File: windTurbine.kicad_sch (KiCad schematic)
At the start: 12 parts, among them M1 Motor_Servo, M2 LP-MSPM0G3507

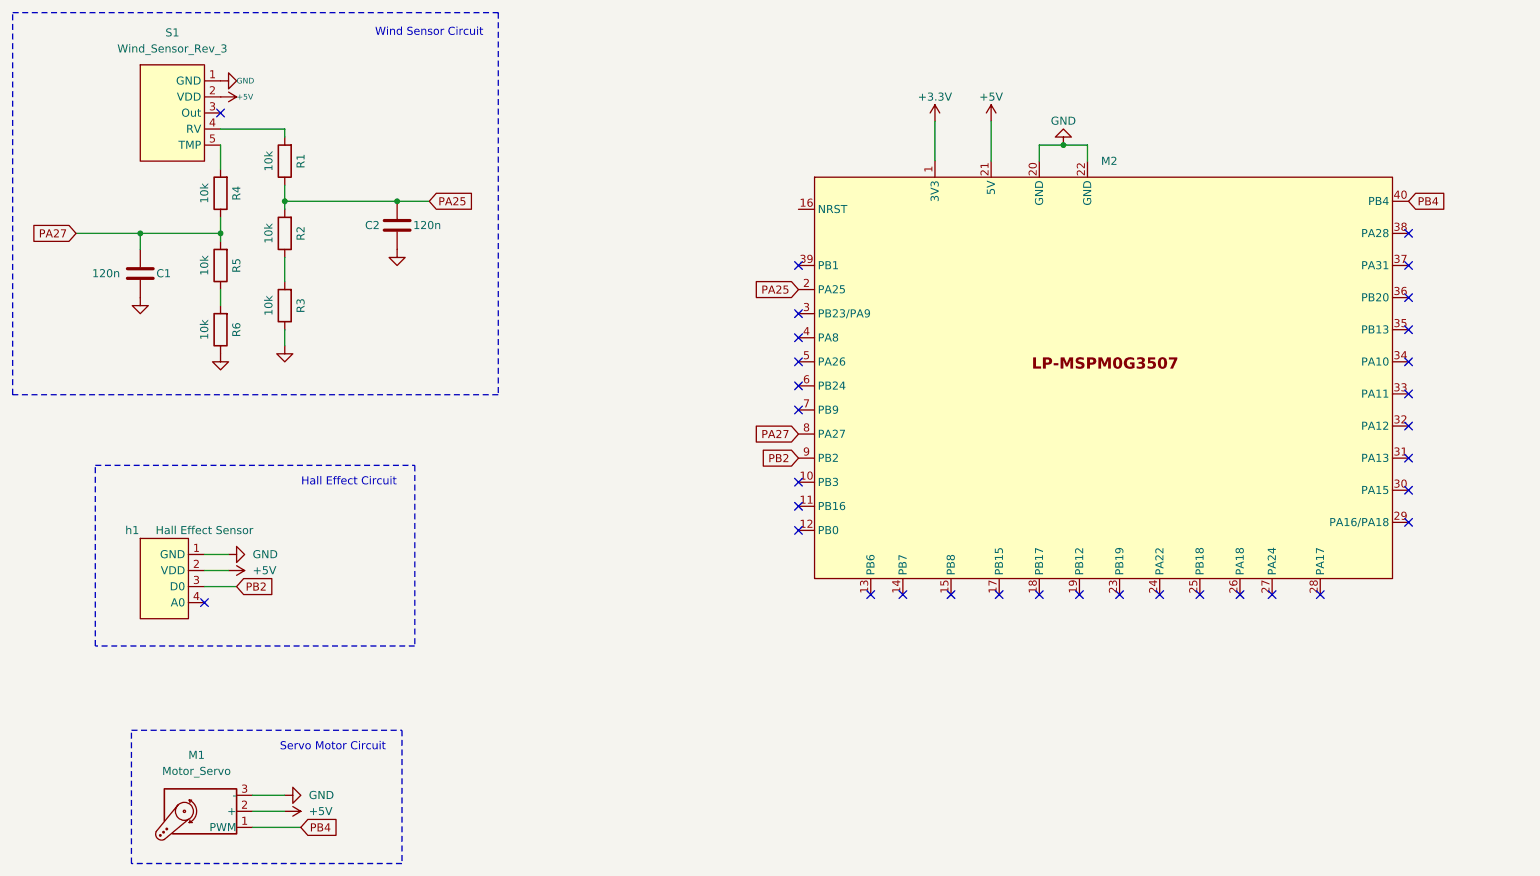
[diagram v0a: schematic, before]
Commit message: Schematic Change. Rearranged Components
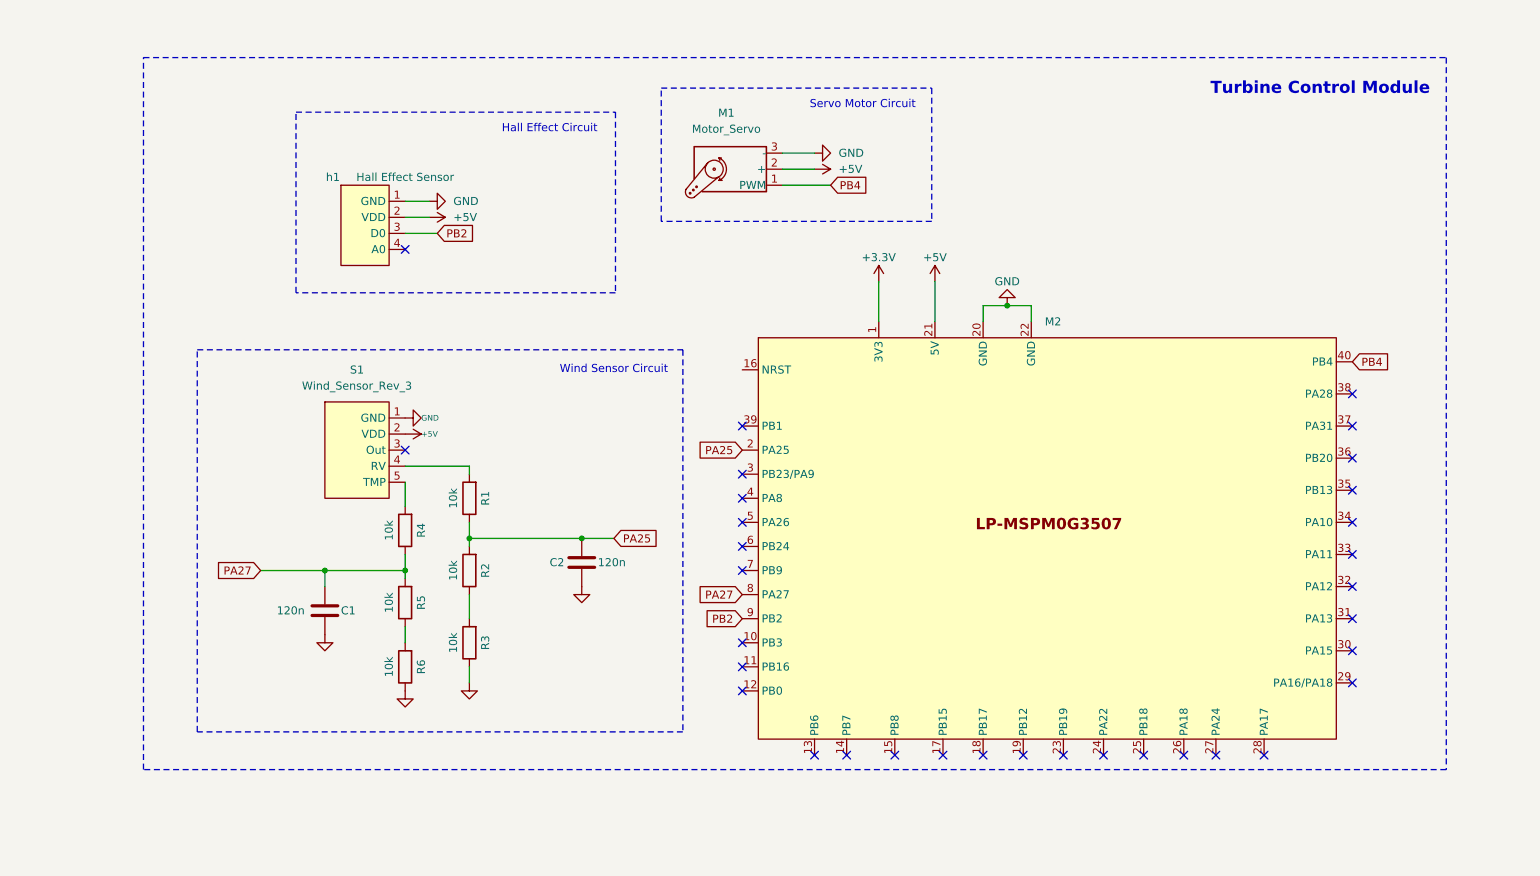
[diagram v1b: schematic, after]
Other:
- note added: "Turbine Control Module"
- moved on the sheet: C1, C2, M1, M2, R1, R2, R3, R4, R5, R6, S1, h1

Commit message: Load MCU
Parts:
- removed C1, C2: 120n, symbol Device:C
- removed M1: Motor_Servo, symbol Motor:Motor_Servo
- removed M2: LP-MSPM0G3507, symbol Turbine_MCU:LP-MSPM0G3507
- removed R1, R2, R3, R4, R5, R6: 10k, symbol Device:R
- removed S1: Wind_Sensor_Rev_3, symbol windTurbineSchemSymLib:Wind_Sensor_Rev_C
- removed h1: Hall Effect Sensor, symbol windTurbineSchemSymLib:hall_effect_sensor
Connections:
- no-connect marks 33 -> 0
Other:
- added sheet Load & MCU Module (load_and_mcu_module.kicad_sch)
- added sheet Turbine Module (turbine_module.kicad_sch)
- note removed: "Hall Effect Circuit"
- note removed: "Servo Motor Circuit"
- note removed: "Turbine Control Module"
- note removed: "Wind Sensor Circuit"

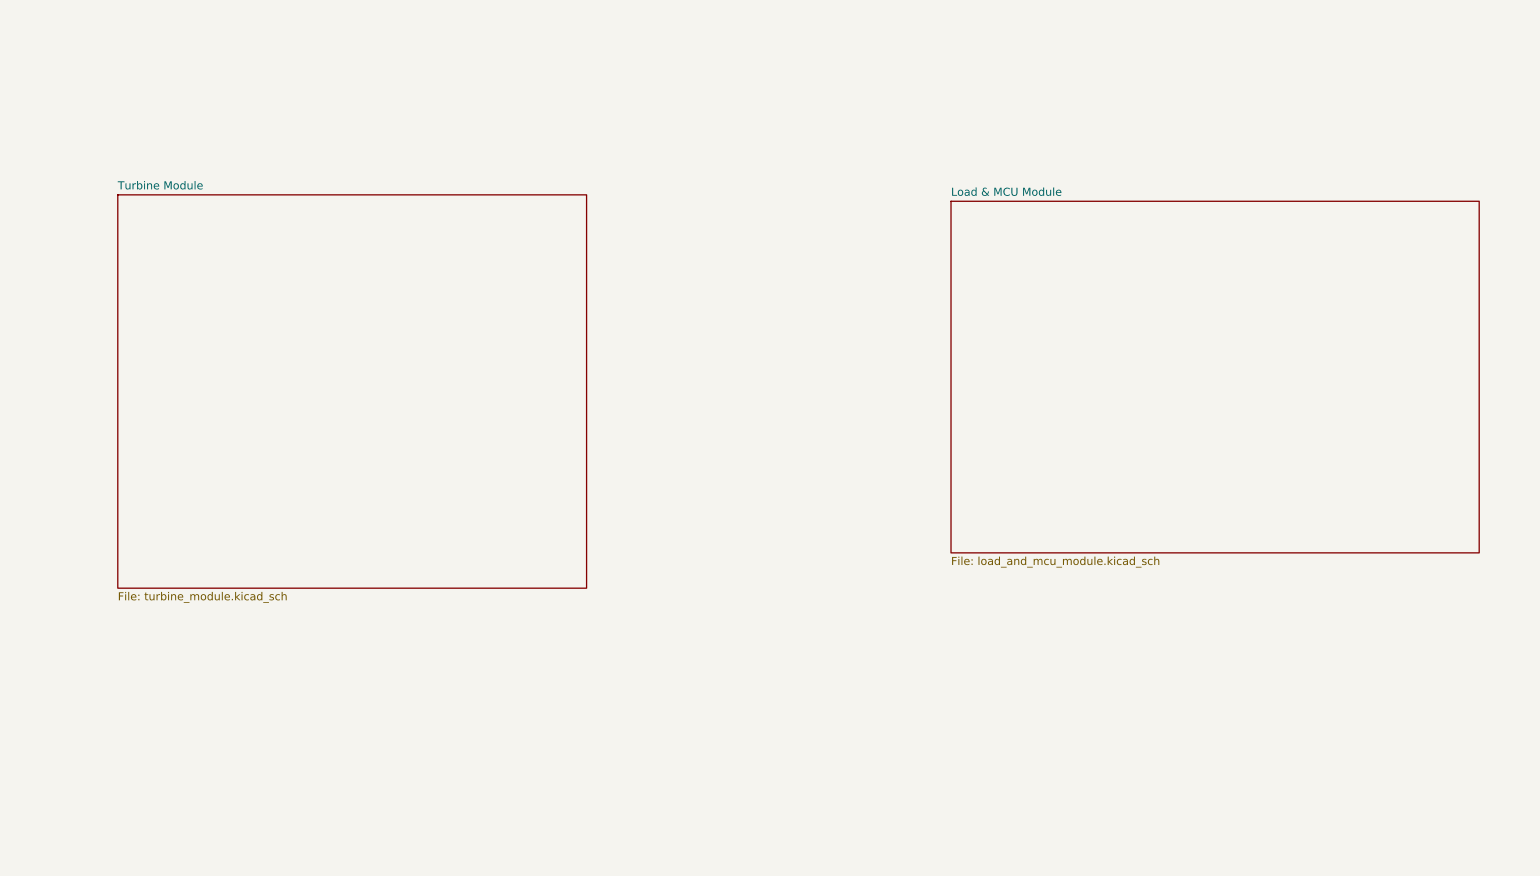
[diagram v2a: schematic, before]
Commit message: Finished Squematics V1
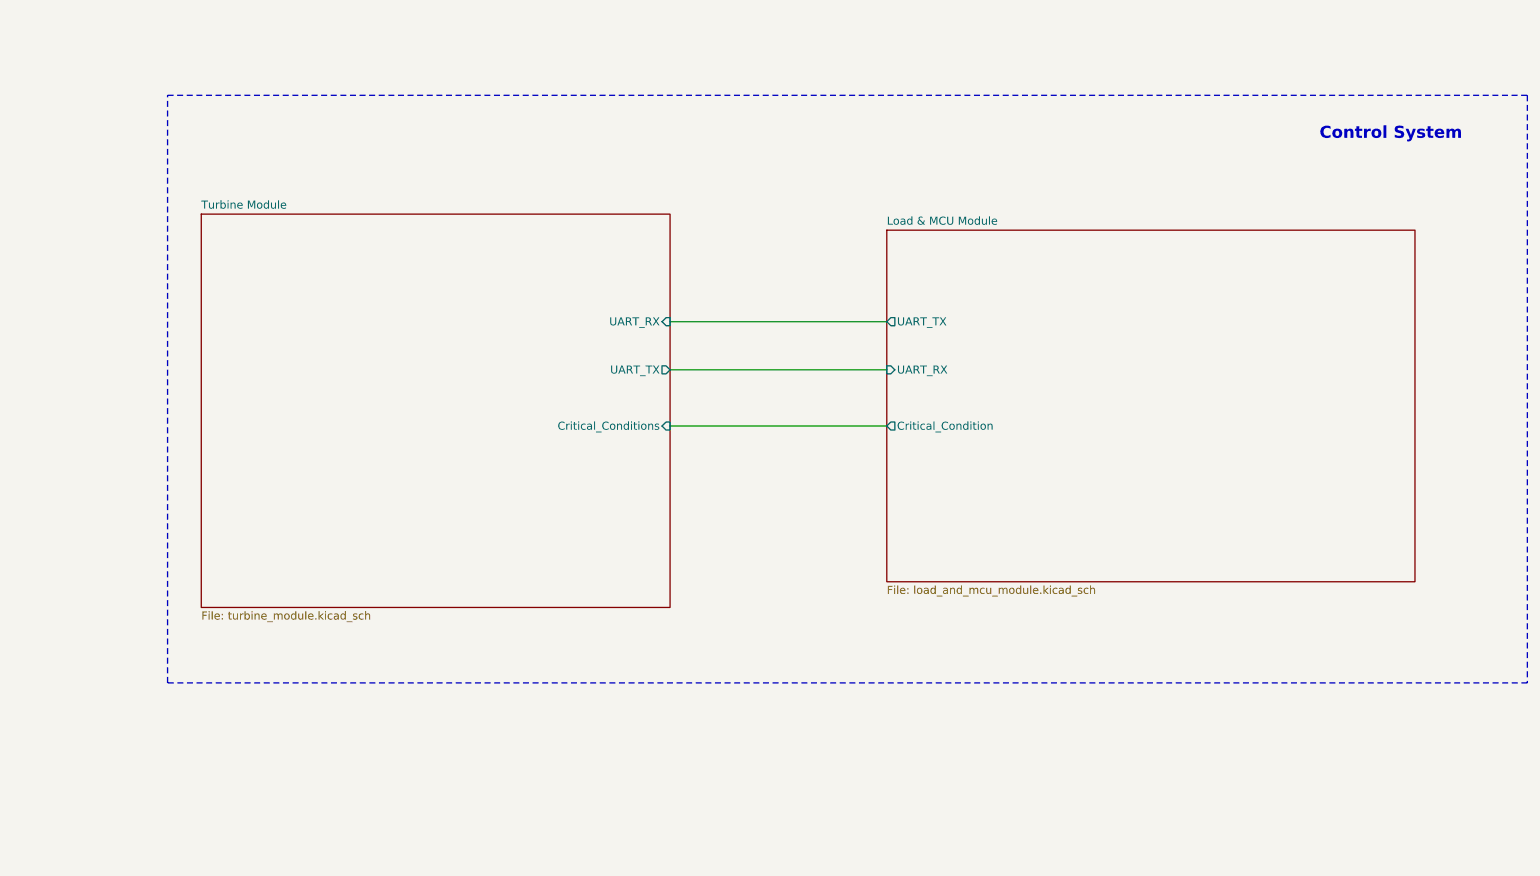
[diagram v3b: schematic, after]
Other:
- sheet Load & MCU Module ports: added Critical_Condition, UART_RX, UART_TX; removed none
- sheet Turbine Module ports: added Critical_Conditions, UART_RX, UART_TX; removed none
- note added: "Control System"
- title: Pitch Control Submodule -> Control System
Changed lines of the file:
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@@
 	(paper "A4")
 	(title_block
-		(title "Pitch Control Submodule")
+		(title "Control System")
 		(date "2026-03-15")
 		(rev "A")
 		(company "Puerto Rico Embedded Solutions")
 	)
+	(rectangle
+		(start 44.958 41.656)
+		(end 260.096 134.62)
+		(stroke
+			(width 0)
+			(type dash)
+		)
+		(fill
+			(type none)
+		)
+	)
+	(text "Control System "
+		(exclude_from_sim no)
+		(at 238.506 47.752 0)
+		(effects
+			(font
+				(size 1.905 1.905)
+				(thickness 0.254)
+				(bold yes)
+			)
+		)
+	)
+	(wire
+		(pts
+			(xy 124.46 85.09) (xy 158.75 85.09)
+		)
+		(stroke
+			(width 0)
+			(type default)
+		)
+	)
+	(wire
+		(pts
+			(xy 124.46 93.98) (xy 158.75 93.98)
+		)
+		(stroke
+			(width 0)
+			(type default)
+		)
+	)
+	(wire
+		(pts
+			(xy 124.46 77.47) (xy 158.75 77.47)
+		)
+		(stroke
+			(width 0)
+			(type default)
+		)
+	)
 	(sheet
-		(at 37.084 57.404)
+		(at 50.292 60.452)
 		(size 74.168 62.23)
 		(exclude_from_sim no)
@@
 		)
 		(property "Sheetname" "Turbine Module"
-			(at 37.084 56.6924 0)
+			(at 50.292 59.7404 0)
 			(effects
 				(font
@@
 		)
 		(property "Sheetfile" "turbine_module.kicad_sch"
-			(at 37.084 120.2186 0)
+			(at 50.292 123.2666 0)
 			(effects
 				(font
@@
 				)
 				(justify left top)
+			)
+		)
+		(pin "UART_RX" input
+			(at 124.46 77.47 0)
+			(effects
+				(font
+					(size 1.27 1.27)
+				)
+				(justify right)
+			)
+		)
+		(pin "UART_TX" output
+			(at 124.46 85.09 0)
+			(effects
+				(font
+					(size 1.27 1.27)
+				)
+				(justify right)
+			)
+		)
+		(pin "Critical_Conditions" input
+			(at 124.46 93.98 0)
+			(effects
+				(font
+					(size 1.27 1.27)
+				)
+				(justify right)
 			)
 		)
@@
 	)
 	(sheet
-		(at 168.91 58.42)
+		(at 158.75 62.992)
 		(size 83.566 55.626)
 		(exclude_from_sim no)
@@
 		)
 		(property "Sheetname" "Load & MCU Module"
-			(at 168.91 57.7084 0)
+			(at 158.75 62.2804 0)
 			(effects
 				(font
@@
 		)
 		(property "Sheetfile" "load_and_mcu_module.kicad_sch"
-			(at 168.91 114.6306 0)
+			(at 158.75 119.2026 0)
 			(effects
 				(font
@@
 			)
 		)
+		(pin "Critical_Condition" output
+			(at 158.75 93.98 180)
+			(effects
+				(font
+					(size 1.27 1.27)
+				)
+				(justify left)
+			)
+		)
+		(pin "UART_RX" input
+			(at 158.75 85.09 180)
+			(effects
+				(font
+					(size 1.27 1.27)
+				)
+				(justify left)
+			)
+		)
+		(pin "UART_TX" output
+			(at 158.75 77.47 180)
+			(effects
+				(font
+					(size 1.27 1.27)
+				)
+				(justify left)
+			)
+		)

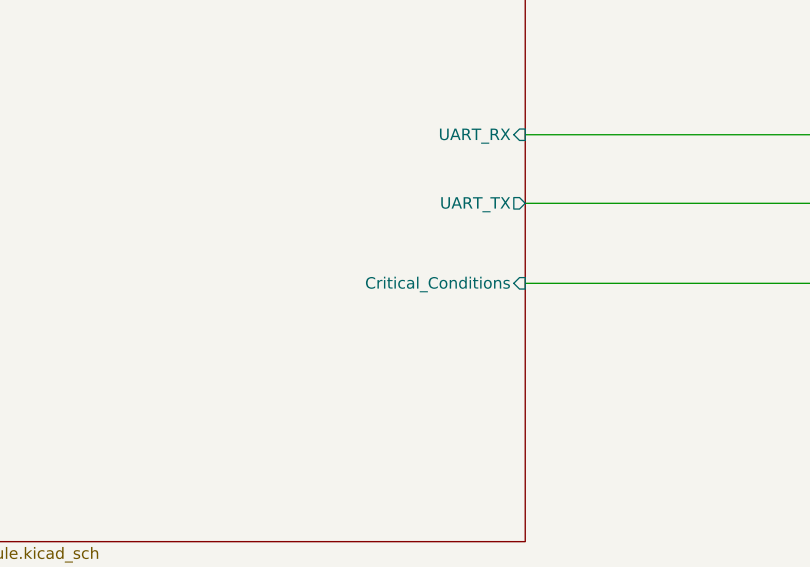
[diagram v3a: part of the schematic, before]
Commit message: Changed a wire name
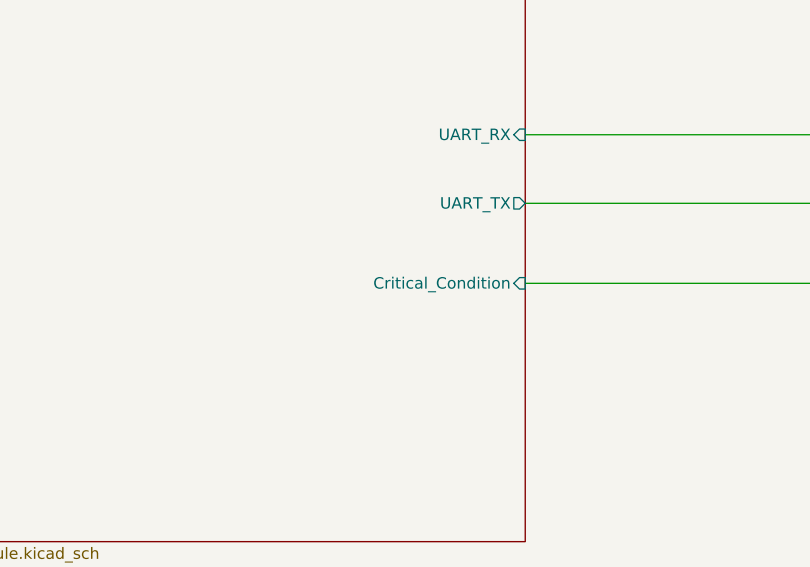
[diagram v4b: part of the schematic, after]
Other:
- sheet Turbine Module ports: added Critical_Condition; removed Critical_Conditions
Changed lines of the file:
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@@
 			)
 		)
-		(pin "Critical_Conditions" input
+		(pin "Critical_Condition" input
 			(at 124.46 93.98 0)
 			(effects

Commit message: Added better colors
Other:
- note added: "Load & UI MCU"
- note added: "Turbine MCU"
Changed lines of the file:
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@@
+		)
+	)
+	(text "Load & UI MCU"
+		(exclude_from_sim no)
+		(at 200.406 91.44 0)
+		(effects
+			(font
+				(size 1.905 1.905)
+				(thickness 0.381)
+				(bold yes)
+				(color 0 0 0 1)
+			)
 		)
 	)
@@
 				(thickness 0.254)
 				(bold yes)
+			)
+		)
+	)
+	(text "Turbine MCU"
+		(exclude_from_sim no)
+		(at 84.328 92.202 0)
+		(effects
+			(font
+				(size 1.905 1.905)
+				(thickness 0.381)
+				(bold yes)
+				(color 0 0 0 1)
 			)
 		)
@@
 		)
 		(fill
-			(color 0 0 0 0.0000)
+			(color 255 255 194 1.0000)
 		)
 		(property "Sheetname" "Turbine Module"
@@
 		)
 		(fill
-			(color 0 0 0 0.0000)
+			(color 255 255 194 1.0000)
 		)
 		(property "Sheetname" "Load & MCU Module"

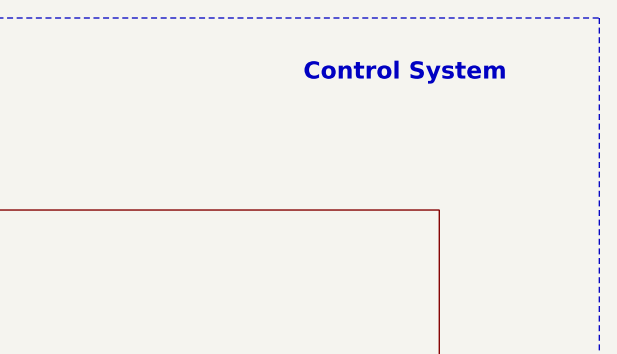
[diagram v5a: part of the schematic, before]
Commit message: converter values adjusted
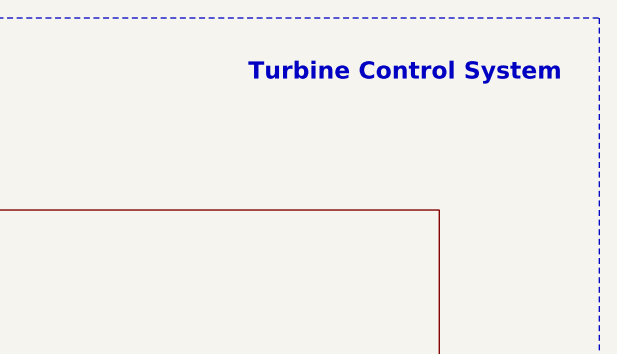
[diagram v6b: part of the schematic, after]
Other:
- note added: "Turbine Control System"
- note removed: "Control System"
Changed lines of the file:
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@@
 		)
 	)
-	(text "Control System "
+	(text "Turbine Control System "
 		(exclude_from_sim no)
 		(at 238.506 47.752 0)
